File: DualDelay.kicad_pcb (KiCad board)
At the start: 2 copper layers, 100 x 83.5 mm, 121 parts, among them J1 IJ/IN/LED/GND/OUT/OJ, J2 INPUT, J3 OUTPUT, J4 DC 9V, SW1 SPDT on-on, U1 PT2399, U2 PT2399, U3 TL072, U4 TL072, U5 TL072, U6 LM358, U7 AMS1117-5.0, U8 AMS1117-5.0

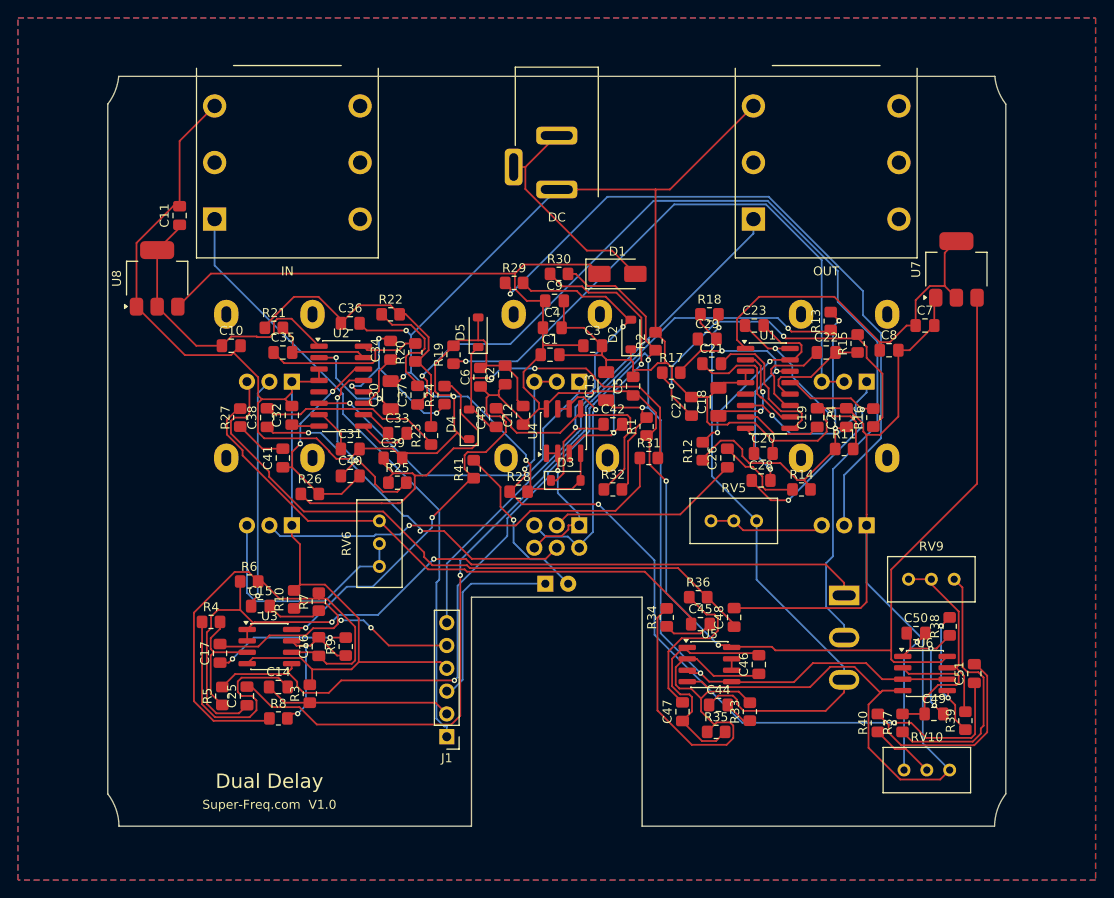
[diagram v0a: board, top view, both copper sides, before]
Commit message: Re-route with the 0.4 mm Power net class restored
Power class in DualDelay.kicad_pro (+9V, GND, V5_1, V5_2, VB, D1-A; Default 0.25 mm), board re-routed
(99 vias, DRC 0/0, parity clean; C32 GND pad solid); buildpcb now restores the .kicad_pro at exit.

Co-Authored-By: Claude Opus 5.5 <noreply@anthropic.com>
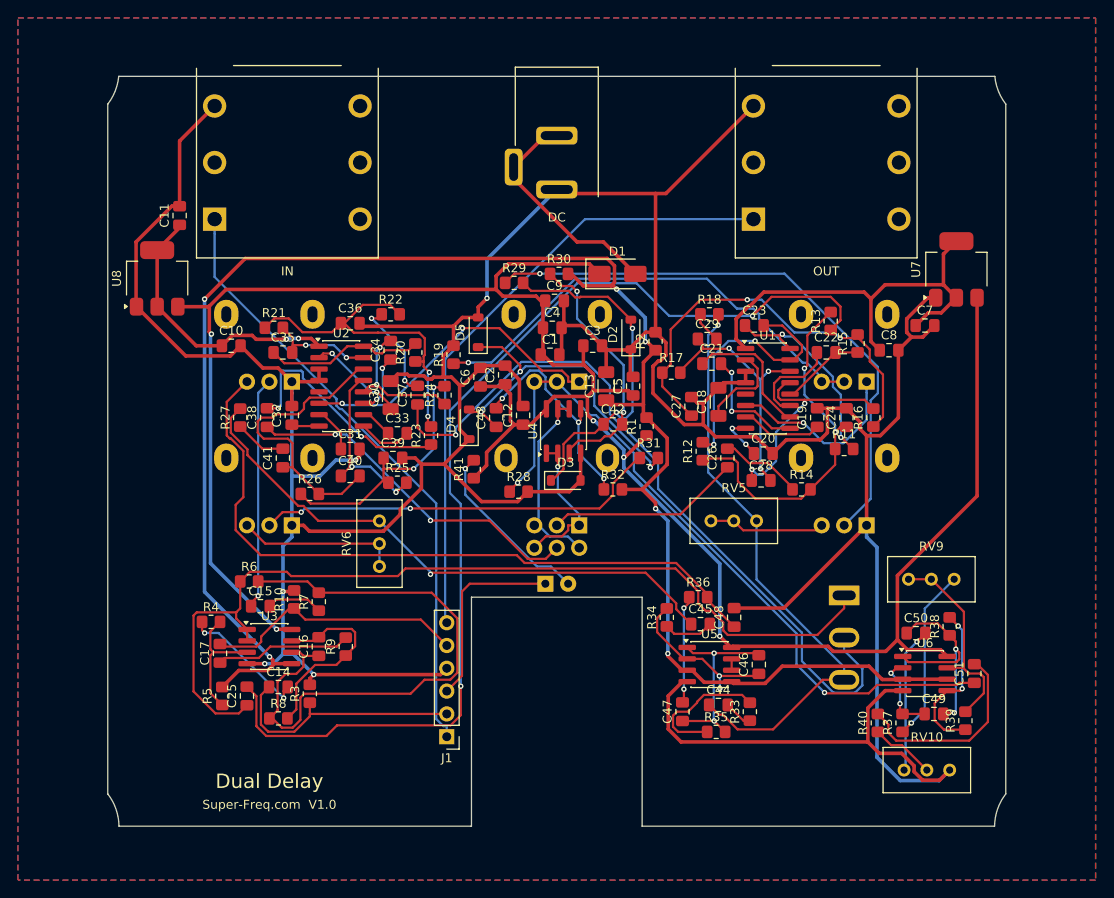
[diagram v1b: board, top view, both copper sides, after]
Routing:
- net /D2IN: track 107.3 -> 83.5 mm
- net Net-(C25-Pad2): track 98.2 -> 118.7 mm
- net /VB: track 175.7 -> 196.2 mm, vias 4 -> 6
- net Net-(U5A--): track 52.7 -> 33.9 mm, vias 0 -> 2
- net /TMIN_1: track 67.0 -> 52.7 mm
- net Net-(U3B--): track 53.8 -> 67.6 mm
- net Net-(R29-Pad1): track 78.2 -> 65.4 mm
- net Net-(C14-Pad2): track 27.0 -> 14.6 mm, vias 0 -> 2
- net /OJ: track 59.1 -> 70.2 mm
- net Net-(C39-Pad1): track 38.0 -> 28.5 mm, vias 0 -> 2
- net Net-(R37-Pad1): track 28.9 -> 19.4 mm, vias 0 -> 1
- net /TMIN_2: track 89.9 -> 80.4 mm, vias 3 -> 2
- net +9V: track 241.5 -> 250.2 mm, vias 4 -> 5
- net /WF2: track 26.8 -> 18.1 mm
- net /LP2O_2: track 25.4 -> 33.5 mm, vias 2 -> 0
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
